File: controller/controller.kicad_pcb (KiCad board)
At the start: 2 copper layers, 59 x 39 mm, 4 parts, among them J1 Conn_01x11_Socket, J2 Conn_01x11_Socket, J3 Conn_01x11_Socket, U1 STM32G474RCTx

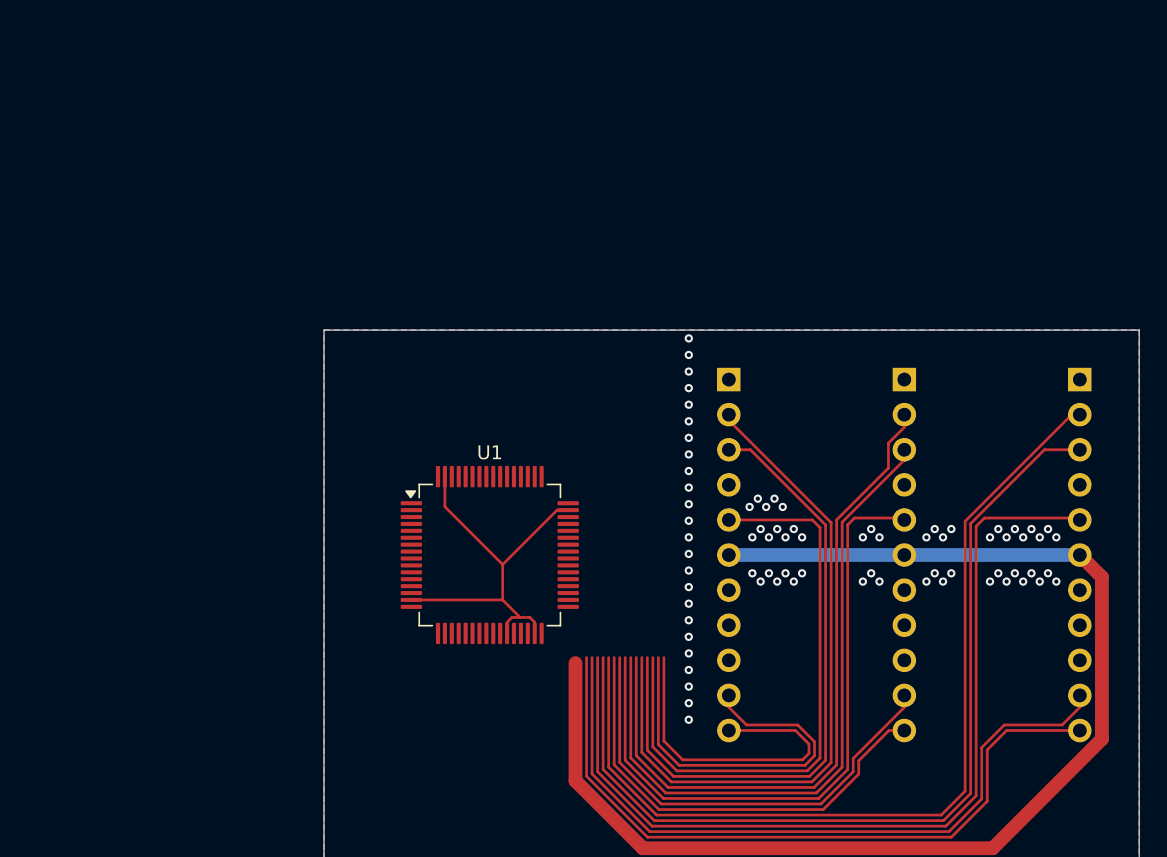
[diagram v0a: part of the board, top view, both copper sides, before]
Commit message: Change pinout and add voltage regulators to controller
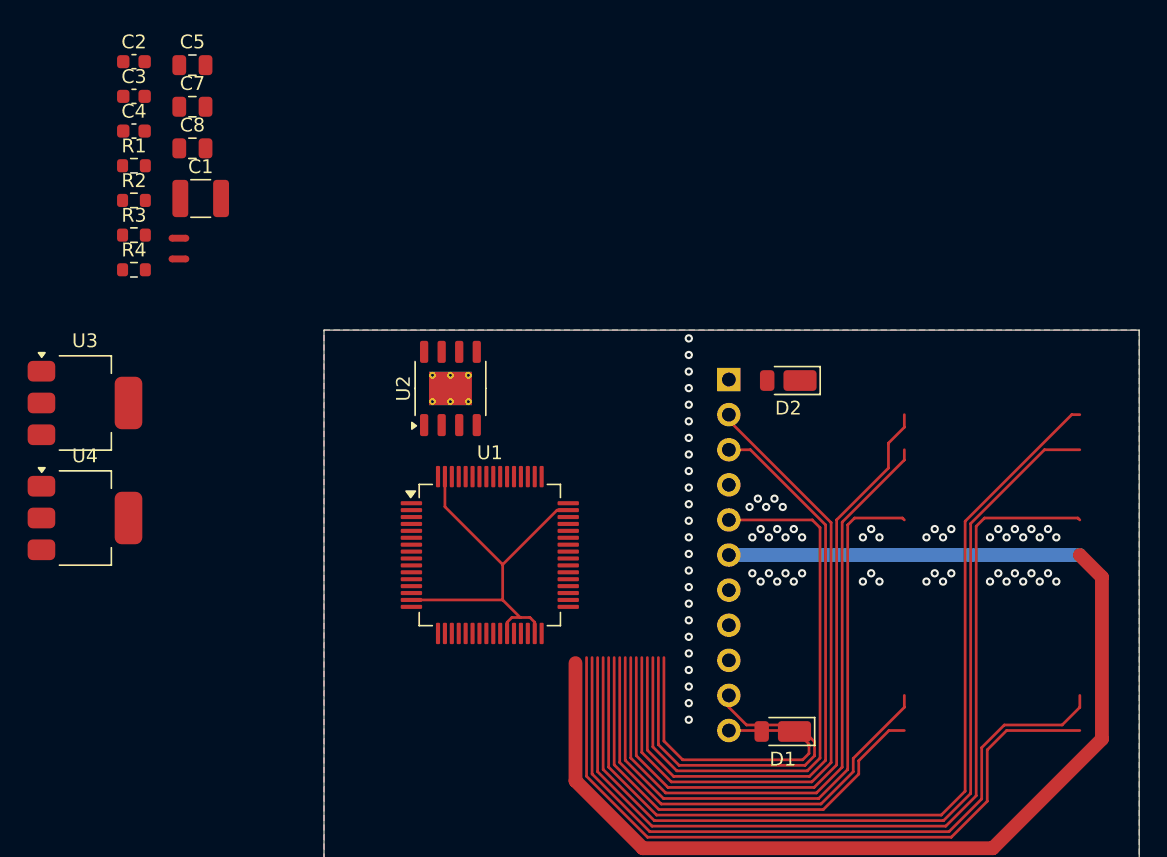
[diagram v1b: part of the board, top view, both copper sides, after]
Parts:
- removed J2, J3: Conn_01x11_Socket, Connector_PinSocket_2.54mm:PinSocket_1x11_P2.54mm_Vertical
- added C1: 2.2uF, Capacitor_SMD:C_1210_3225Metric, F.Cu at (76.1, 55.5)
- added C2: 2.2nF, Capacitor_SMD:C_0603_1608Metric, F.Cu at (71.2, 45.6)
- added C3: 1.2nF, Capacitor_SMD:C_0603_1608Metric, F.Cu at (71.2, 48.1)
- added C4: 47pF, Capacitor_SMD:C_0603_1608Metric, F.Cu at (71.2, 50.6)
- added C5: 4.7uF, Capacitor_SMD:C_0805_2012Metric, F.Cu at (75.5, 45.8)
- added C7: 4.7uF, Capacitor_SMD:C_0805_2012Metric, F.Cu at (75.5, 48.8)
- added C8: 4.7uF, Capacitor_SMD:C_0805_2012Metric, F.Cu at (75.5, 51.8)
- added D1: DFLS1200, Diode_SMD:D_PowerDI-123, F.Cu at (118.2, 94.0)
- added D2: DFLS1200, Diode_SMD:D_PowerDI-123, F.Cu at (118.6, 68.7)
- added NT1: NetTie_2, NetTie:NetTie-2_SMD_Pad0.5mm, F.Cu at (74.5, 58.4)
- added NT2: NetTie_2, NetTie:NetTie-2_SMD_Pad0.5mm, F.Cu at (74.5, 59.9)
- added R1: 121k, Resistor_SMD:R_0603_1608Metric, F.Cu at (71.2, 53.1)
- added R2: 576k, Resistor_SMD:R_0603_1608Metric, F.Cu at (71.2, 55.6)
- added R3: 101k, Resistor_SMD:R_0603_1608Metric, F.Cu at (71.2, 58.1)
- added R4: 66.5k, Resistor_SMD:R_0603_1608Metric, F.Cu at (71.2, 60.6)
- added U2: LM5168, Package_SO:HSOP-8-1EP_3.9x4.9mm_P1.27mm_EP2.41x3.1mm_ThermalVias, F.Cu at (94.2, 69.2)
- added U3: TLV76133DCY, Package_TO_SOT_SMD:SOT-223-3_TabPin2, F.Cu at (67.7, 70.3)
- added U4: TLV76150DCY, Package_TO_SOT_SMD:SOT-223-3_TabPin2, F.Cu at (67.7, 78.6)
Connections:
- net Current_sense-_1 renamed Current_sense_1
- J1 pad 1: Earth -> FB_LOW_1
- J1 pad 10: /LI_1 -> /HI_1
- J1 pad 11: /HI_1 -> FB_HIGH_1
- J1 pad 2: Current_sense+_1 -> Earth
- J1 pad 5: FB_HIGH_1 -> 6-18V
- J1 pad 6: 6-18V -> NTC_1
- J1 pad 7: +5V -> Net-(J1-Pin_7)
- J1 pad 9: Earth -> /LI_1
- U1 pad 16: unconnected-(U1-VDD-Pad16) -> +3V3
- U1 pad 28: unconnected-(U1-VREF+-Pad28) -> +3V3
- U1 pad 29: unconnected-(U1-VDDA-Pad29) -> +3V3
- U1 pad 32: unconnected-(U1-VDD-Pad32) -> +3V3
- U1 pad 48: unconnected-(U1-VDD-Pad48) -> +3V3
- U1 pad 64: unconnected-(U1-VDD-Pad64) -> +3V3
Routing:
- net (no net): track 0.00 -> 517.1 mm
- net Current_sense+_3: track 66.9 -> 0.00 mm
- net Current_sense-_3: track 66.7 -> 0.00 mm
- net FB_HIGH_3: track 65.5 -> 0.00 mm
- net /LI_3: track 52.2 -> 0.00 mm
- net /HI_3: track 51.5 -> 0.00 mm
- net Current_sense+_2: track 50.6 -> 0.00 mm
- net Earth: track 29.3 -> 79.6 mm
- net Current_sense+_1: track 50.3 -> 0.00 mm
- net Current_sense-_2: track 49.2 -> 0.00 mm
- net FB_HIGH_2: track 47.6 -> 0.00 mm
- net /LI_2: track 33.8 -> 0.00 mm
- net /HI_2: track 33.0 -> 0.00 mm
- net /LI_1: track 27.6 -> 0.00 mm
- net NTC_1: track 0.00 -> 25.4 mm
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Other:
- copper layers 2 -> 4

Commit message: Controller - Add labels for pin functions
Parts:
- added D3: DFLS1200, Diode_SMD:D_PowerDI-123, F.Cu at (64.0, 110.5)
- added D4: DFLS1200, Diode_SMD:D_PowerDI-123, F.Cu at (64.0, 114.1)
- added J2: USB_C_Receptacle_USB2.0_16P, Connector_USB:USB_C_Receptacle_GCT_USB4105-xx-A_16P_TopMnt_Horizontal, F.Cu at (45.4, 95.4)
- added J3: USB_C_Receptacle_PowerOnly_6P, Connector_USB:USB_C_Receptacle_GCT_USB4105-xx-A_16P_TopMnt_Horizontal, F.Cu at (45.4, 105.4)
- added J4: Conn_01x03_Pin, TestPoint:TestPoint_2Pads_Pitch5.08mm_Drill1.3mm, F.Cu at (53.5, 111.0)
- added J5: Conn_01x03_Pin, TestPoint:TestPoint_2Pads_Pitch5.08mm_Drill1.3mm, F.Cu at (53.5, 115.6)
- added U6: STM32G474VETx, Package_QFP:LQFP-100_14x14mm_P0.5mm, F.Cu at (66.2, 81.5)
- added U7: STM32G474METx, Package_QFP:LQFP-80_12x12mm_P0.5mm, F.Cu at (82.6, 81.3)
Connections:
- U1 pad 12: unconnected-(U1-PA0-Pad12) -> COMP3_INP
- U1 pad 13: unconnected-(U1-PA1-Pad13) -> COMP1_INP
- U1 pad 24: unconnected-(U1-PB0-Pad24) -> COMP4_INP
- U1 pad 25: unconnected-(U1-PB1-Pad25) -> COMP1_INP
- U1 pad 33: unconnected-(U1-PB11-Pad33) -> COMP6_INP
- U1 pad 34: unconnected-(U1-PB12-Pad34) -> HRTIM1_CHC1
- U1 pad 35: unconnected-(U1-PB13-Pad35) -> HRTIM1_CHC2
- U1 pad 36: unconnected-(U1-PB14-Pad36) -> HRTIM1_CHD1
- U1 pad 37: unconnected-(U1-PB15-Pad37) -> HRTIM1_CHD2
- U1 pad 38: unconnected-(U1-PC6-Pad38) -> HRTIM1_CHF1
- U1 pad 39: unconnected-(U1-PC7-Pad39) -> HRTIM1_CHF2
- U1 pad 40: unconnected-(U1-PC8-Pad40) -> HRTIM1_CHE1
- U1 pad 41: unconnected-(U1-PC9-Pad41) -> HRTIM1_CHE2
- U1 pad 42: unconnected-(U1-PA8-Pad42) -> HRTIM1_CHA1
- U1 pad 43: unconnected-(U1-PA9-Pad43) -> HRTIM1_CHA2
- U1 pad 44: unconnected-(U1-PA10-Pad44) -> HRTIM1_CHB1
- U1 pad 45: unconnected-(U1-PA11-Pad45) -> HRTIM1_CHB2
- U1 pad 46: unconnected-(U1-PA12-Pad46) -> USB_D+
- U1 pad 56: unconnected-(U1-PB3-Pad56) -> HRTIM1_EEV9
- U1 pad 57: unconnected-(U1-PB4-Pad57) -> HRTIM1_EEV7
- U1 pad 58: unconnected-(U1-PB5-Pad58) -> HRTIM1_EEV6
- U1 pad 59: unconnected-(U1-PB6-Pad59) -> HRTIM1_EEV4
- U1 pad 60: unconnected-(U1-PB7-Pad60) -> HRTIM1_EEV3
- U1 pad 62: unconnected-(U1-PB9-Pad62) -> HRTIM1_EEV5
- U1 pad 9: unconnected-(U1-PC1-Pad9) -> COMP3_INP

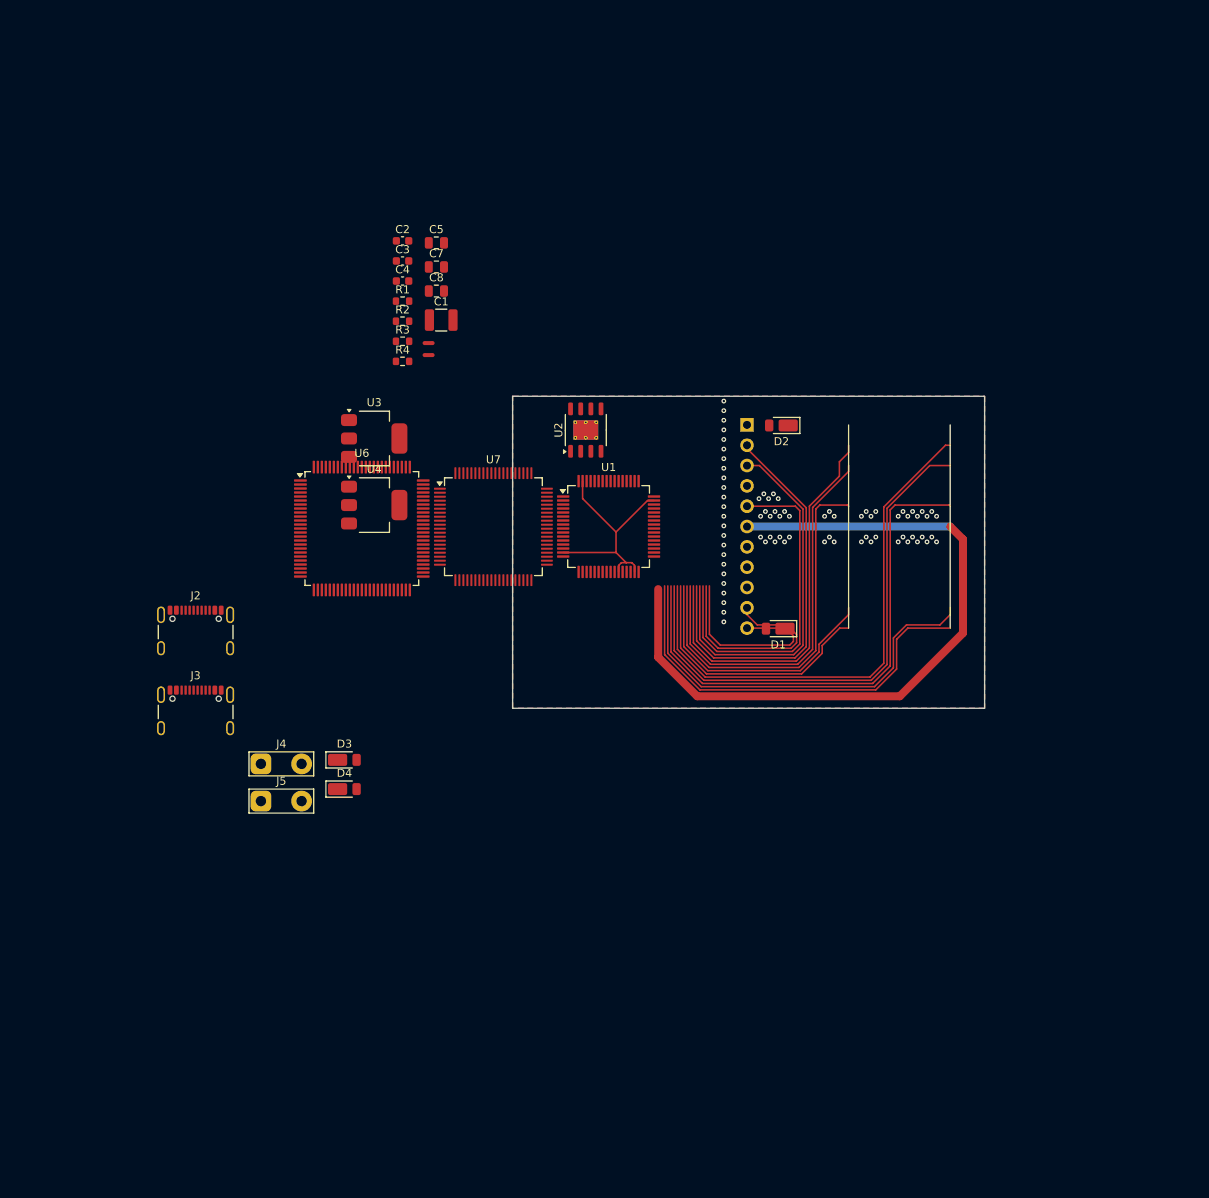
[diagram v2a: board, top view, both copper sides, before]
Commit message: Fixup reference designators, more work on controller etc
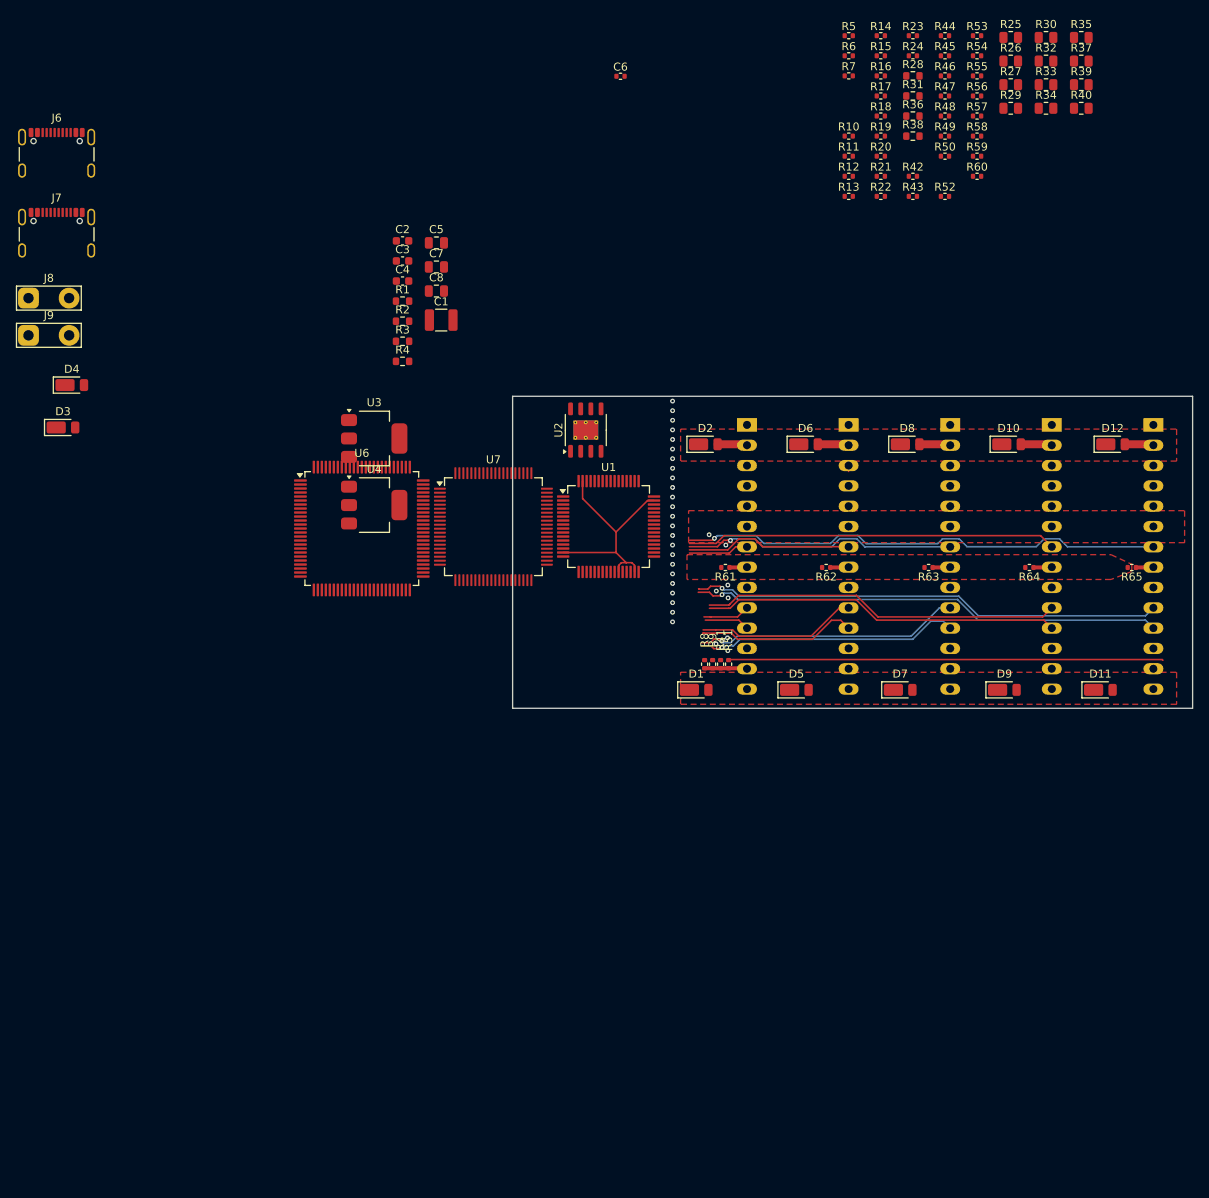
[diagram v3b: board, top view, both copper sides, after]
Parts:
- removed NT1, NT2: NetTie_2, NetTie:NetTie-2_SMD_Pad0.5mm
- added C6: 2.2uF, Resistor_SMD:R_0402_1005Metric, F.Cu at (98.5, 25.0)
- added D10: DFLS1200, Diode_SMD:D_PowerDI-123, F.Cu at (147.0, 71.0)
- added D11: DFLS1200, Diode_SMD:D_PowerDI-123, F.Cu at (158.5, 101.7)
- added D12: DFLS1200, Diode_SMD:D_PowerDI-123, F.Cu at (160.0, 71.0)
- added D5: DFLS1200, Diode_SMD:D_PowerDI-123, F.Cu at (120.5, 101.7)
- added D6: DFLS1200, Diode_SMD:D_PowerDI-123, F.Cu at (121.6, 71.0)
- added D7: DFLS1200, Diode_SMD:D_PowerDI-123, F.Cu at (133.4, 101.7)
- added D8: DFLS1200, Diode_SMD:D_PowerDI-123, F.Cu at (134.3, 71.0)
- added D9: DFLS1200, Diode_SMD:D_PowerDI-123, F.Cu at (146.5, 101.7)
- added J6: USB_C_Receptacle_USB2.0_16P, Connector_USB:USB_C_Receptacle_GCT_USB4105-xx-A_16P_TopMnt_Horizontal, F.Cu at (28.0, 35.7)
- added J7: USB_C_Receptacle_PowerOnly_6P, Connector_USB:USB_C_Receptacle_GCT_USB4105-xx-A_16P_TopMnt_Horizontal, F.Cu at (28.0, 45.7)
- added J8: Conn_01x03_Pin, TestPoint:TestPoint_2Pads_Pitch5.08mm_Drill1.3mm, F.Cu at (24.5, 52.7)
- added J9: Conn_01x03_Pin, TestPoint:TestPoint_2Pads_Pitch5.08mm_Drill1.3mm, F.Cu at (24.5, 57.4)
- added R10: 0R, Resistor_SMD:R_0402_1005Metric, F.Cu at (127.0, 32.5)
- added R11: 0R, Resistor_SMD:R_0402_1005Metric, F.Cu at (127.0, 35.0)
- added R12: 0R, Resistor_SMD:R_0402_1005Metric, F.Cu at (127.0, 37.5)
- added R13: 0R, Resistor_SMD:R_0402_1005Metric, F.Cu at (127.0, 40.0)
- added R14: 0R, Resistor_SMD:R_0402_1005Metric, F.Cu at (131.0, 19.9)
- added R15: 0R, Resistor_SMD:R_0402_1005Metric, F.Cu at (131.0, 22.4)
- added R16: 0R, Resistor_SMD:R_0402_1005Metric, F.Cu at (131.0, 24.9)
- added R17: 0R, Resistor_SMD:R_0402_1005Metric, F.Cu at (131.0, 27.5)
- added R18: 0R, Resistor_SMD:R_0402_1005Metric, F.Cu at (131.0, 30.0)
- added R19: 0R, Resistor_SMD:R_0402_1005Metric, F.Cu at (131.0, 32.5)
- added R20: 0R, Resistor_SMD:R_0402_1005Metric, F.Cu at (131.0, 35.0)
- added R21: 0R, Resistor_SMD:R_0402_1005Metric, F.Cu at (131.0, 37.5)
- added R22: 0R, Resistor_SMD:R_0402_1005Metric, F.Cu at (131.0, 40.0)
- added R23: 0R, Resistor_SMD:R_0402_1005Metric, F.Cu at (135.0, 19.9)
- added R24: 0R, Resistor_SMD:R_0402_1005Metric, F.Cu at (135.0, 22.4)
- added R25: R_Small, Resistor_SMD:R_0805_2012Metric, F.Cu at (147.3, 20.1)
- added R26: R_Small, Resistor_SMD:R_0805_2012Metric, F.Cu at (147.3, 23.1)
- added R27: R_Small, Resistor_SMD:R_0805_2012Metric, F.Cu at (147.3, 26.1)
- added R28: R_Small, Resistor_SMD:R_0603_1608Metric, F.Cu at (135.0, 24.9)
- added R29: R_Small, Resistor_SMD:R_0805_2012Metric, F.Cu at (147.3, 29.0)
- added R30: R_Small, Resistor_SMD:R_0805_2012Metric, F.Cu at (151.7, 20.1)
- added R31: R_Small, Resistor_SMD:R_0603_1608Metric, F.Cu at (135.0, 27.5)
- added R32: R_Small, Resistor_SMD:R_0805_2012Metric, F.Cu at (151.7, 23.1)
- added R33: R_Small, Resistor_SMD:R_0805_2012Metric, F.Cu at (151.7, 26.1)
- added R34: R_Small, Resistor_SMD:R_0805_2012Metric, F.Cu at (151.7, 29.0)
- added R35: R_Small, Resistor_SMD:R_0805_2012Metric, F.Cu at (156.1, 20.1)
- added R36: R_Small, Resistor_SMD:R_0603_1608Metric, F.Cu at (135.0, 30.0)
- added R37: R_Small, Resistor_SMD:R_0805_2012Metric, F.Cu at (156.1, 23.1)
- added R38: R_Small, Resistor_SMD:R_0603_1608Metric, F.Cu at (135.0, 32.5)
- added R39: R_Small, Resistor_SMD:R_0805_2012Metric, F.Cu at (156.1, 26.1)
- added R40: R_Small, Resistor_SMD:R_0805_2012Metric, F.Cu at (156.1, 29.0)
- added R41: 0R, Resistor_SMD:R_0402_1005Metric, F.Cu at (111.0, 98.5)
- added R42: 0R, Resistor_SMD:R_0402_1005Metric, F.Cu at (135.0, 37.5)
- added R43: 0R, Resistor_SMD:R_0402_1005Metric, F.Cu at (135.0, 40.0)
- added R44: 0R, Resistor_SMD:R_0402_1005Metric, F.Cu at (139.0, 19.9)
- added R45: 0R, Resistor_SMD:R_0402_1005Metric, F.Cu at (139.0, 22.4)
- added R46: 0R, Resistor_SMD:R_0402_1005Metric, F.Cu at (139.0, 24.9)
- added R47: 0R, Resistor_SMD:R_0402_1005Metric, F.Cu at (139.0, 27.5)
- added R48: 0R, Resistor_SMD:R_0402_1005Metric, F.Cu at (139.0, 30.0)
- added R49: 0R, Resistor_SMD:R_0402_1005Metric, F.Cu at (139.0, 32.5)
- added R5: 0R, Resistor_SMD:R_0402_1005Metric, F.Cu at (127.0, 19.9)
- added R50: 0R, Resistor_SMD:R_0402_1005Metric, F.Cu at (139.0, 35.0)
- added R51: 0R, Resistor_SMD:R_0402_1005Metric, F.Cu at (112.0, 98.5)
- added R52: 0R, Resistor_SMD:R_0402_1005Metric, F.Cu at (139.0, 40.0)
- added R53: 0R, Resistor_SMD:R_0402_1005Metric, F.Cu at (143.1, 19.9)
- added R54: 0R, Resistor_SMD:R_0402_1005Metric, F.Cu at (143.1, 22.4)
- added R55: 0R, Resistor_SMD:R_0402_1005Metric, F.Cu at (143.1, 24.9)
- added R56: 0R, Resistor_SMD:R_0402_1005Metric, F.Cu at (143.1, 27.5)
- added R57: 0R, Resistor_SMD:R_0402_1005Metric, F.Cu at (143.1, 30.0)
- added R58: 0R, Resistor_SMD:R_0402_1005Metric, F.Cu at (143.1, 32.5)
- added R59: 0R, Resistor_SMD:R_0402_1005Metric, F.Cu at (143.1, 35.0)
- added R6: 0R, Resistor_SMD:R_0402_1005Metric, F.Cu at (127.0, 22.4)
- added R60: 0R, Resistor_SMD:R_0402_1005Metric, F.Cu at (143.1, 37.5)
- added R61: 0R, Resistor_SMD:R_0402_1005Metric, F.Cu at (111.6, 86.4)
- added R62: 0R, Resistor_SMD:R_0402_1005Metric, F.Cu at (124.2, 86.4)
- added R63: 0R, Resistor_SMD:R_0402_1005Metric, F.Cu at (137.0, 86.4)
- added R64: 0R, Resistor_SMD:R_0402_1005Metric, F.Cu at (149.6, 86.4)
- added R65: 0R, Resistor_SMD:R_0402_1005Metric, F.Cu at (162.4, 86.4)
- added R7: 0R, Resistor_SMD:R_0402_1005Metric, F.Cu at (127.0, 24.9)
- added R8: 0R, Resistor_SMD:R_0402_1005Metric, F.Cu at (109.0, 98.5)
- added R9: 0R, Resistor_SMD:R_0402_1005Metric, F.Cu at (110.0, 98.5)
- J1: value Conn_01x11_Socket -> Conn_01x14; footprint Connector_PinSocket_2.54mm:PinSocket_1x11_P2.54mm_Vertical -> Library:half_bridge_card
- J2: value USB_C_Receptacle_USB2.0_16P -> Conn_01x14; footprint Connector_USB:USB_C_Receptacle_GCT_USB4105-xx-A_16P_TopMnt_Horizontal -> Library:half_bridge_card; moved to B.Cu
- J3: value USB_C_Receptacle_PowerOnly_6P -> Conn_01x14; footprint Connector_USB:USB_C_Receptacle_GCT_USB4105-xx-A_16P_TopMnt_Horizontal -> Library:half_bridge_card; moved to B.Cu
- J4, J5: value Conn_01x03_Pin -> Conn_01x14; footprint TestPoint:TestPoint_2Pads_Pitch5.08mm_Drill1.3mm -> Library:half_bridge_card; moved to B.Cu
- moved J5 121.1 mm to (165.1, 68.6), turned to 180 degrees
- moved J4 107.6 mm to (152.4, 68.6), turned to 180 degrees
- moved J3 101.3 mm to (139.7, 68.6), turned to 180 degrees
- moved J2 85.9 mm to (127.0, 68.6), turned to 180 degrees
- moved D4 60.9 mm to (29.9, 63.6)
- moved D3 54.4 mm to (28.8, 68.9)
- moved D1 12.8 mm to (108.0, 101.7), turned to 0 degrees
- moved D2 9.79 mm to (109.1, 71.0), turned to 0 degrees
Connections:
- net HRTIM1_CHA2 renamed UCPD1_DBCC1
- net HRTIM1_CHB1 renamed UCPD1_DBCC2
- net HRTIM1_CHB2 renamed USB_D-
- net HRTIM1_EEV4 renamed UCPD1_CC1
- net HRTIM1_EEV7 renamed UCPD1_CC2
- net HRTIM1_EEV9 renamed UCPD1_CRS_SYNC
- C3 pad 1: 8v -> 6-18V
- C5 pad 1: 8v -> 6-18V
- D1 pad 2: FB_HIGH_1 -> Net-(D1-A)
- D2 pad 2: FB_LOW_1 -> Net-(D2-A)
- J1 pad 1: FB_LOW_1 -> Earth
- J1 pad 10: /HI_1 -> /LI_1
- J1 pad 11: FB_HIGH_1 -> /HI_1
- J1 pad 2: Earth -> Net-(D2-A)
- J1 pad 3: Current_sense_1 -> Earth
- J1 pad 4: Earth -> Current_sense_1
- J1 pad 5: 6-18V -> Earth
- J1 pad 6: NTC_1 -> 6-18V
- J1 pad 7: Net-(J1-Pin_7) -> NTC_1
- J1 pad 8: Earth -> Net-(J1-Pin_8)
- J1 pad 9: /LI_1 -> Earth
- J4 pad 1: FB_LOW -> Earth
- J4 pad 2: Net-(D3-A) -> Net-(D10-A)
- J5 pad 1: FB_LOW -> Earth
- J5 pad 2: Net-(D4-A) -> Net-(D12-A)
- R2 pad 1: 8v -> 6-18V
- U1 pad 11: unconnected-(U1-PC3-Pad11) -> OPAMP5_VINP
- U1 pad 13: COMP1_INP -> OPAMP1_VINP
- U1 pad 14: unconnected-(U1-PA2-Pad14) -> UCPD1_FRSTX__1
- U1 pad 17: unconnected-(U1-PA3-Pad17) -> COMP2_INP
- U1 pad 19: unconnected-(U1-PA5-Pad19) -> UCPD1_FRSTX__2
- U1 pad 21: unconnected-(U1-PA7-Pad21) -> OPAMP2_VINP
- U1 pad 23: unconnected-(U1-PC5-Pad23) -> HRTIM1_EEV10
- U1 pad 61: unconnected-(U1-PB8-Pad61) -> BOOT0
- U3 pad 3: 8v -> 6-18V
- U4 pad 3: 8v -> 6-18V
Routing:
- net (no net): track 517.1 -> 0.00 mm
- net 6-18V: track 109.1 -> 0.00 mm
- net NTC_5: track 0.00 -> 61.0 mm, vias 0 -> 1
- net /HI_5: track 0.00 -> 59.0 mm, vias 0 -> 1
- net /LI_5: track 0.00 -> 59.0 mm, vias 0 -> 1
- net FB_D_FULL: track 0.00 -> 54.4 mm
- net Earth: track 79.6 -> 30.5 mm, vias 75 -> 32
- net Current_sense_1: track 47.2 -> 0.00 mm
- net NTC_4: track 0.00 -> 46.3 mm
- net /LI_4: track 0.00 -> 44.9 mm
- net /HI_4: track 0.00 -> 44.7 mm
- net NTC_3: track 0.00 -> 34.6 mm, vias 0 -> 1
- net /LI_3: track 0.00 -> 33.6 mm, vias 0 -> 1
- net /HI_3: track 0.00 -> 33.3 mm, vias 0 -> 1
- net FB_HIGH_1: track 24.2 -> 0.00 mm
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- added copper zone on F.Cu, net +5V
- added copper zone on F.Cu, net 6-18V
- added copper zone on In1.Cu, net Earth
- added copper zone on In2.Cu, net Earth
- added copper zone on F.Cu, net Logic DC/DC in
- removed copper zone on B.Cu, net Earth
- removed copper zone on F.Cu, net Earth
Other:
- board size 59 x 39 mm -> 85 x 39 mm
